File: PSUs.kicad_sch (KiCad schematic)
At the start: 33 parts, among them J19 Barrel_Jack, J20 AMP171826-4, Q1 DMP3013SFV-7, U16 AP64501SP-13

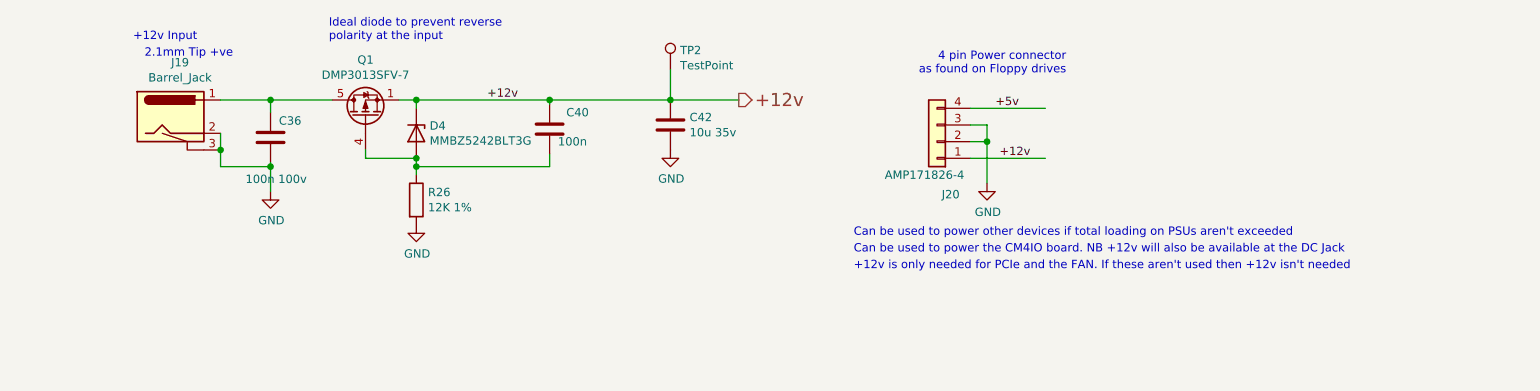
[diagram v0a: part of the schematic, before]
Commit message: removed many unused parts
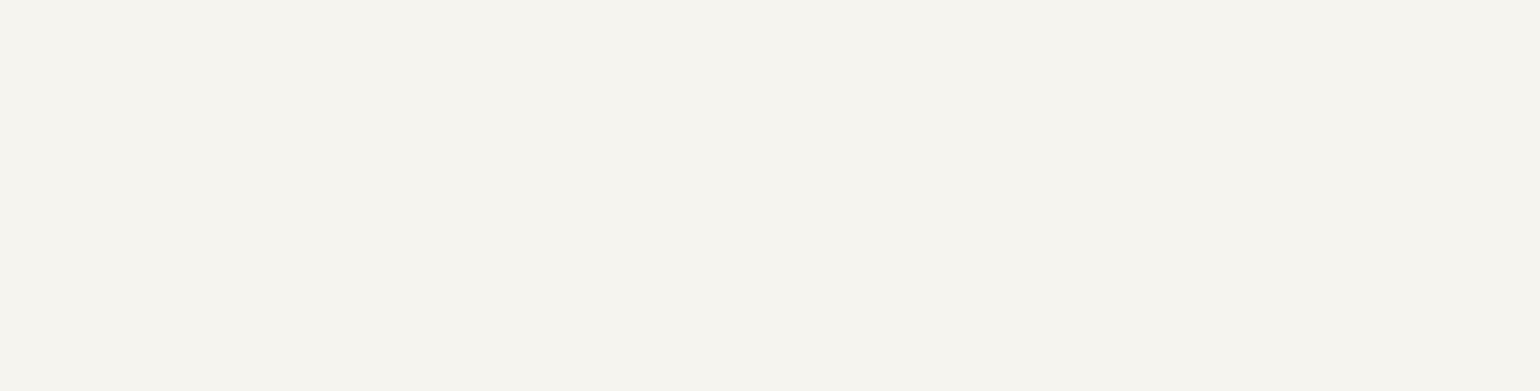
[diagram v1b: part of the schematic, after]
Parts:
- removed C36: 100n 100v, Capacitor_SMD:C_0402_1005Metric, symbol Device:C
- removed C40: 100n, Capacitor_SMD:C_0402_1005Metric, symbol Device:C
- removed C42: 10u 35v, Capacitor_SMD:C_0805_2012Metric, symbol Device:C
- removed D4: MMBZ5242BLT3G, Diode_SMD:D_SOT-23_ANK, symbol Diode:BZX84Cxx
- removed J19: Barrel_Jack, Connector_BarrelJack:BarrelJack_Horizontal, symbol CM4IO:Barrel_Jack
- removed J20: AMP171826-4, 171826-4:TE_171826-4, symbol Connector_Generic:Conn_01x04
- removed Q1: DMP3013SFV-7, Package_SON:Diodes_PowerDI3333-8, symbol Transistor_FET:DMP3013SFV
- removed R26: 12K 1%, Resistor_SMD:R_0402_1005Metric, symbol Device:R
- removed TP2: TestPoint, TestPoint:TestPoint_Pad_2.0x2.0mm, symbol Connector:TestPoint
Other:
- note removed: "+12v Input"
- note removed: "+12v is only needed for PCIe and the FAN. If these aren't used then +12v isn't needed"
- note removed: "2.1mm Tip +ve"
- note removed: "4 pin Power connector as found on Floppy drives"
- note removed: "Can be used to power other devices if total loading on PSUs aren't exceeded"
- note removed: "Can be used to power the CM4IO board. NB +12v will also be available at the DC Jack"
- note removed: "Ideal diode to prevent reverse polarity at the input"
- company: © 2020-2022 Raspberry Pi Ltd (formerly Raspberry Pi (Trading) Ltd.) -> (none)
- title: Compute Module 4 IO Board - PSUs -> bitcart - PSUs
